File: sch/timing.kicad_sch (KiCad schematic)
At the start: 18 parts

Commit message: Sch: video block rework
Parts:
- D33: value 74S04 -> (none); CCCP (none) -> КР531ЛН1
- D37: value ~ -> (none); CCCP (none) -> К155ЛИ1
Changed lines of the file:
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@@
     (in_bom yes) (on_board yes)
     (property "Reference" "D37" (id 0) (at 253.365 147.32 0))
-    (property "Value" "~" (id 1) (at 254.635 146.685 0))
+    (property "Value" "" (id 1) (at 254.635 146.685 0))
     (property "Footprint" "" (id 2) (at 254.635 153.035 0)
       (effects (font (size 1.27 1.27)) hide)
     )
     (property "Datasheet" "http://www.ti.com/lit/gpn/sn74LS08" (id 3) (at 254.635 153.035 0)
+      (effects (font (size 1.27 1.27)) hide)
+    )
+    (property "CCCP" "К155ЛИ1" (id 4) (at 97.155 76.2 0)
       (effects (font (size 1.27 1.27)) hide)
     )
@@
     (in_bom yes) (on_board yes)
     (property "Reference" "D33" (id 0) (at 41.275 59.055 0))
-    (property "Value" "74S04" (id 1) (at 41.275 61.595 0))
+    (property "Value" "" (id 1) (at 41.275 61.595 0))
     (property "Footprint" "" (id 2) (at 41.275 67.945 0)
       (effects (font (size 1.27 1.27)) hide)
@@
       (effects (font (size 1.27 1.27)) hide)
     )
+    (property "CCCP" "КР531ЛН1" (id 4) (at 80.645 78.74 0))
     (pin "1")
     (pin "2")
@@
     (in_bom yes) (on_board yes)
     (property "Reference" "D37" (id 0) (at 260.985 62.865 0))
-    (property "Value" "~" (id 1) (at 262.255 50.165 0))
+    (property "Value" "" (id 1) (at 262.255 50.165 0))
     (property "Footprint" "" (id 2) (at 262.255 56.515 0)
       (effects (font (size 1.27 1.27)) hide)
@@
       (effects (font (size 1.27 1.27)) hide)
     )
+    (property "CCCP" "К155ЛИ1" (id 4) (at 97.155 76.2 0)
+      (effects (font (size 1.27 1.27)) hide)
+    )

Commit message: Sch: video block cleanup in progress
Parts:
- D33: value (none) -> 74S04
- D37: value (none) -> 7408
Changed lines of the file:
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@@
     (in_bom yes) (on_board yes)
     (property "Reference" "D37" (id 0) (at 253.365 147.32 0))
-    (property "Value" "" (id 1) (at 254.635 146.685 0))
+    (property "Value" "7408" (id 1) (at 254.635 146.685 0))
     (property "Footprint" "" (id 2) (at 254.635 153.035 0)
       (effects (font (size 1.27 1.27)) hide)
@@
     (in_bom yes) (on_board yes)
     (property "Reference" "D33" (id 0) (at 41.275 59.055 0))
-    (property "Value" "" (id 1) (at 41.275 61.595 0))
+    (property "Value" "74S04" (id 1) (at 41.275 61.595 0))
     (property "Footprint" "" (id 2) (at 41.275 67.945 0)
       (effects (font (size 1.27 1.27)) hide)
@@
     (in_bom yes) (on_board yes)
     (property "Reference" "D37" (id 0) (at 260.985 62.865 0))
-    (property "Value" "" (id 1) (at 262.255 50.165 0))
+    (property "Value" "7408" (id 1) (at 262.255 50.165 0))
     (property "Footprint" "" (id 2) (at 262.255 56.515 0)
       (effects (font (size 1.27 1.27)) hide)

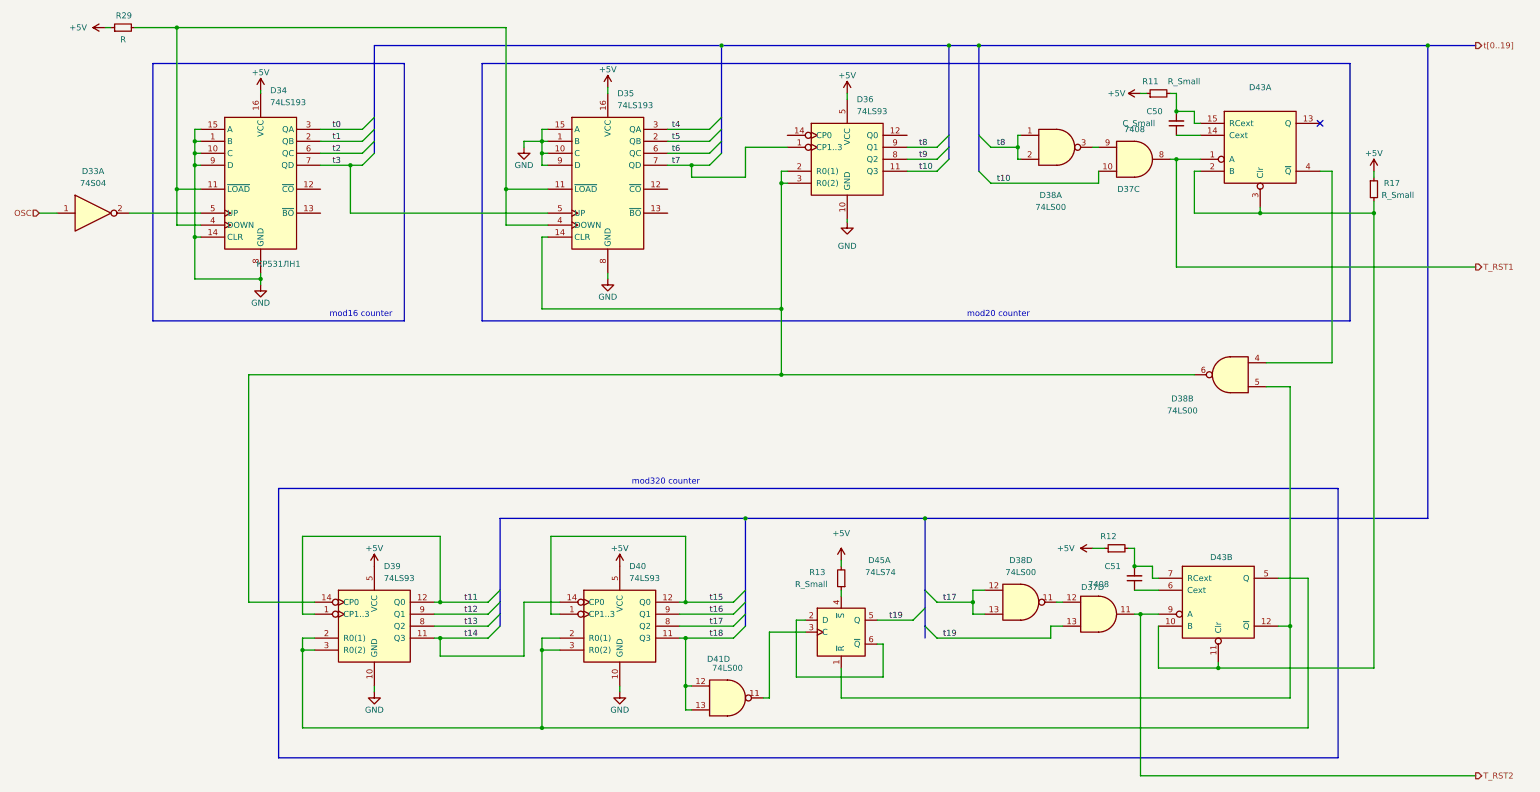
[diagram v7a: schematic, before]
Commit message: Sch: timing block completed
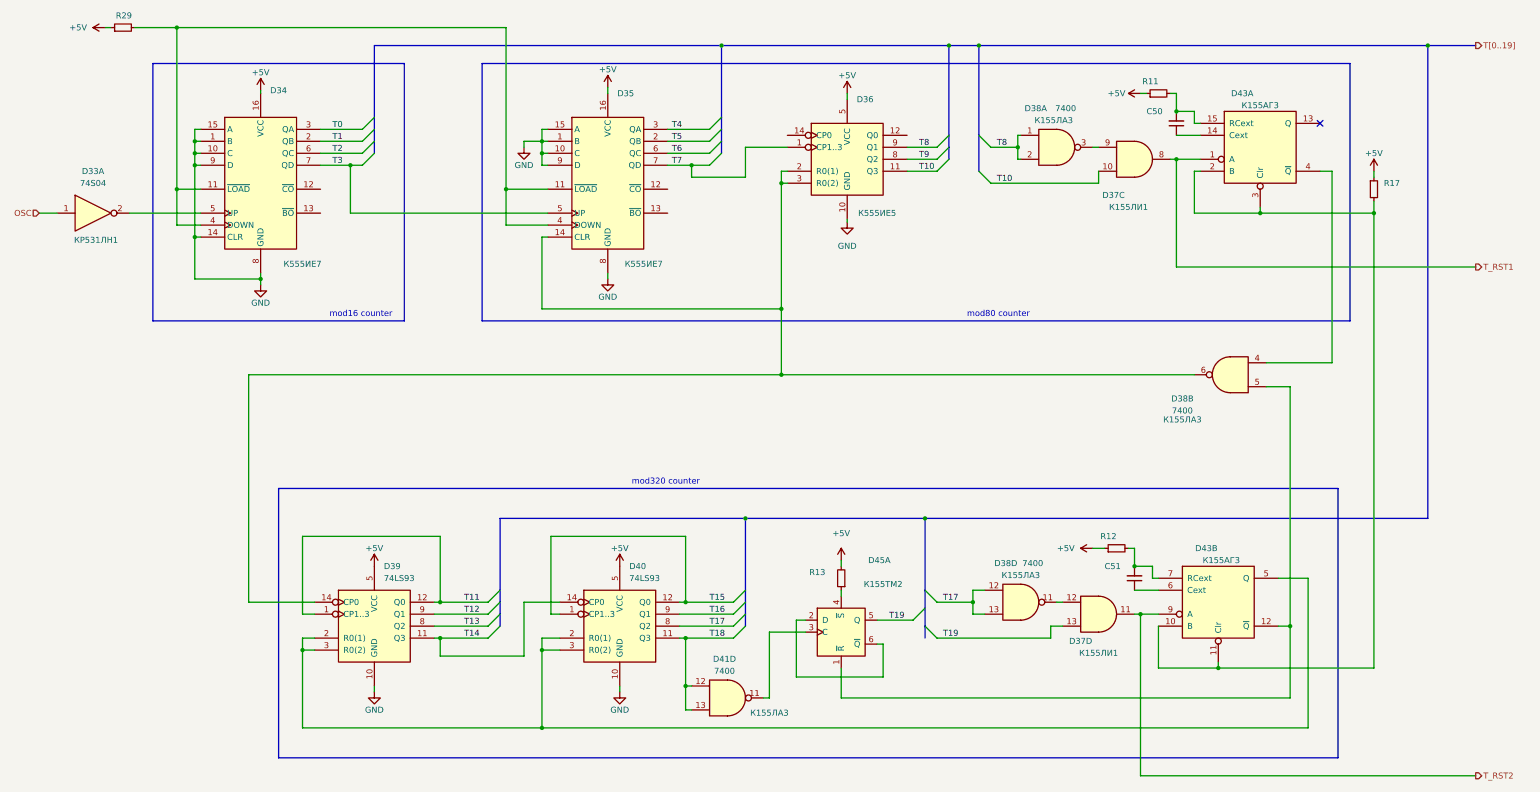
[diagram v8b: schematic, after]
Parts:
- C50: value C_Small -> (none)
- C51, R12: value ~ -> (none)
- D34, D35: value 74LS193 -> (none); CCCP (none) -> К555ИЕ7
- D36: value 74LS93 -> (none); CCCP (none) -> К555ИЕ5
- D37: value 7408 -> (none)
- D38, D41: value 74LS00 -> 7400; CCCP (none) -> К155ЛА3
- D43: value ~ -> (none); CCCP (none) -> К155АГ3
- D45: value 74LS74 -> (none); CCCP (none) -> К155ТМ2
- R11, R13, R17: value R_Small -> (none)
- R29: value R -> (none)
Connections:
- net t0 renamed T0
- net t1 renamed T1
- net t10 renamed T10
- net t11 renamed T11
- net t12 renamed T12
- net t13 renamed T13
- net t14 renamed T14
- net t15 renamed T15
- net t16 renamed T16
- net t17 renamed T17
- net t18 renamed T18
- net t19 renamed T19
- net t2 renamed T2
- net t3 renamed T3
- net t4 renamed T4
- net t5 renamed T5
- net t6 renamed T6
- net t7 renamed T7
- net t8 renamed T8
- net t9 renamed T9
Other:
- note added: "mod80 counter"
- note removed: "mod20 counter"
